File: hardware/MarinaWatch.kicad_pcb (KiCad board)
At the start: 2 copper layers, 45.4 x 40.5 mm, 18 parts, among them J1 USB_C_Receptacle_USB2.0_16P, J2 Screw_Terminal_01x02, U1 ESP32-S3-MINI-1, U2 MCP73831-2-OT, U3 AP2112K-3.3

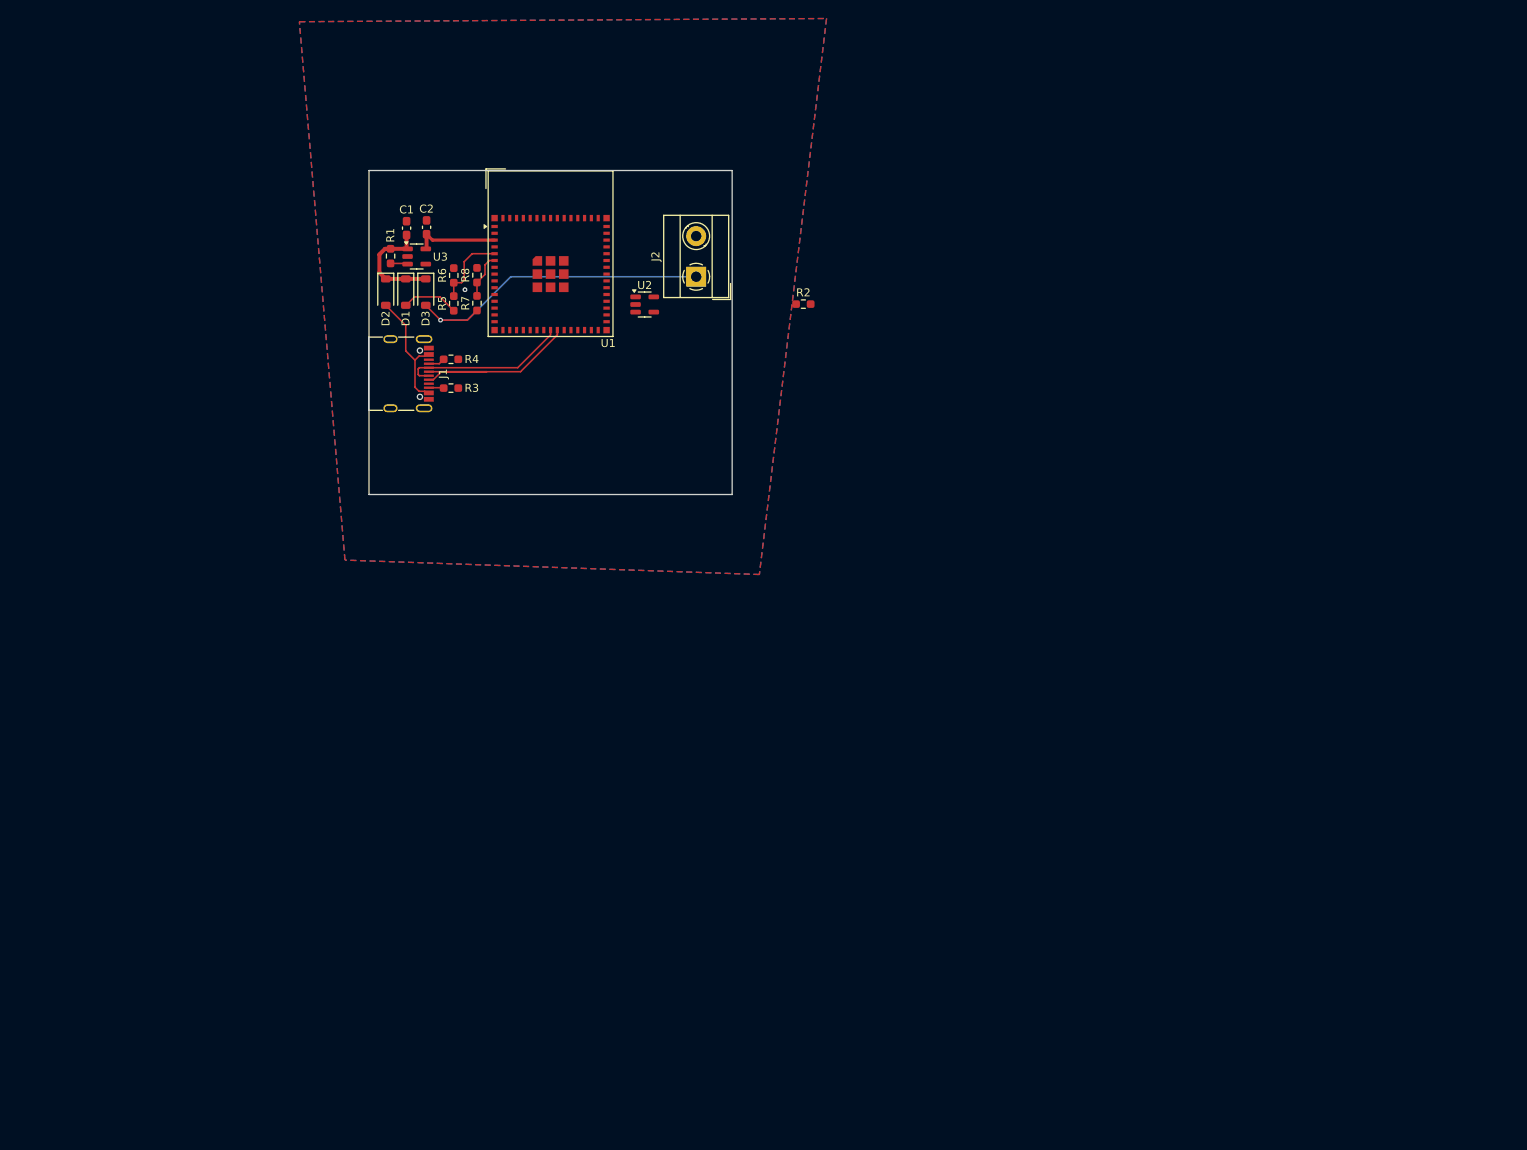
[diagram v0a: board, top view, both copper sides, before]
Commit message: Started with footprints and layout
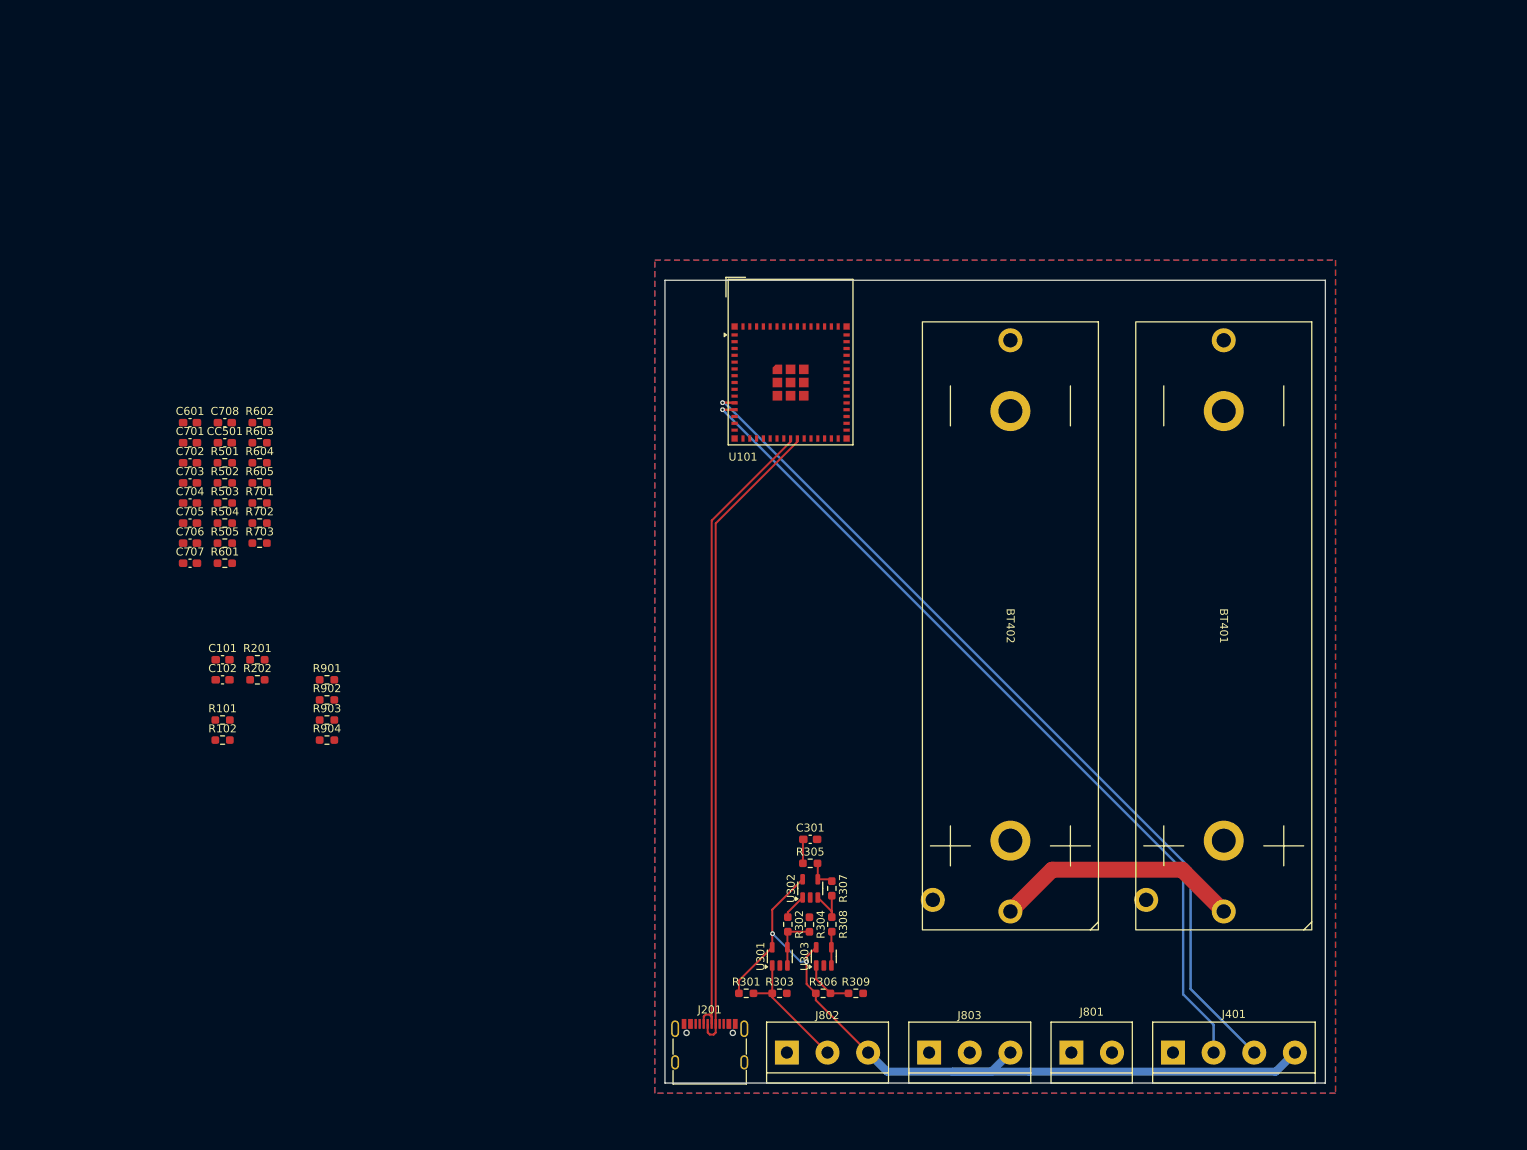
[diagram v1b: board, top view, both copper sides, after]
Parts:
- removed C1, C2: 10u, Capacitor_SMD:C_0603_1608Metric_Pad1.08x0.95mm_HandSolder
- removed D1, D2, D3: 1N5819, Diode_SMD:D_SOD-123
- removed J1: USB_C_Receptacle_USB2.0_16P, Connector_USB:USB_C_Receptacle_G-Switch_GT-USB-7010ASV
- removed J2: Screw_Terminal_01x02, TerminalBlock_MetzConnect:TerminalBlock_MetzConnect_Type101_RT01602HBWC_1x02_P5.08mm_Horizontal
- removed R1, R2: 12k, Resistor_SMD:R_0603_1608Metric_Pad0.98x0.95mm_HandSolder
- removed R3, R4, R5, R6, R7, R8: 5k1, Resistor_SMD:R_0603_1608Metric_Pad0.98x0.95mm_HandSolder
- removed U1: ESP32-S3-MINI-1, RF_Module:ESP32-S2-MINI-1
- removed U2: MCP73831-2-OT, Package_TO_SOT_SMD:SOT-23-5
- removed U3: AP2112K-3.3, Package_TO_SOT_SMD:SOT-23-5
- added BT401: Battery_Cell, AlfredLib:18650, F.Cu at (184.2, 96.5)
- added BT402: Battery_Cell, AlfredLib:18650, F.Cu at (157.5, 96.5)
- added C101: 10u, Capacitor_SMD:C_0603_1608Metric_Pad1.08x0.95mm_HandSolder, F.Cu at (59.0, 100.8)
- added C102: 10u, Capacitor_SMD:C_0603_1608Metric_Pad1.08x0.95mm_HandSolder, F.Cu at (59.0, 103.3)
- added C301: 22u, Capacitor_SMD:C_0603_1608Metric_Pad1.08x0.95mm_HandSolder, F.Cu at (132.5, 123.2)
- added C601: 10u, Capacitor_SMD:C_0603_1608Metric_Pad1.08x0.95mm_HandSolder, F.Cu at (54.9, 71.1)
- added C701: 10u, Capacitor_SMD:C_0603_1608Metric_Pad1.08x0.95mm_HandSolder, F.Cu at (54.9, 73.6)
- added C702: 10u, Capacitor_SMD:C_0603_1608Metric_Pad1.08x0.95mm_HandSolder, F.Cu at (54.9, 76.1)
- added C703: 10u, Capacitor_SMD:C_0603_1608Metric_Pad1.08x0.95mm_HandSolder, F.Cu at (54.9, 78.7)
- added C704: 10u, Capacitor_SMD:C_0603_1608Metric_Pad1.08x0.95mm_HandSolder, F.Cu at (54.9, 81.2)
- added C705: 22u, Capacitor_SMD:C_0603_1608Metric_Pad1.08x0.95mm_HandSolder, F.Cu at (54.9, 83.7)
- added C706: 22u, Capacitor_SMD:C_0603_1608Metric_Pad1.08x0.95mm_HandSolder, F.Cu at (54.9, 86.2)
- added C707: 22u, Capacitor_SMD:C_0603_1608Metric_Pad1.08x0.95mm_HandSolder, F.Cu at (54.9, 88.7)
- added C708: 100n, Capacitor_SMD:C_0603_1608Metric_Pad1.08x0.95mm_HandSolder, F.Cu at (59.3, 71.1)
- added CC501: 10u, Capacitor_SMD:C_0603_1608Metric_Pad1.08x0.95mm_HandSolder, F.Cu at (59.3, 73.6)
- added J201: USB_C_Receptacle_USB2.0_16P, Connector_USB:USB_C_Receptacle_G-Switch_GT-USB-7010ASV, F.Cu at (119.9, 150.0)
- added J401: Screw_Terminal_01x04, TerminalBlock:TerminalBlock_bornier-4_P5.08mm, F.Cu at (177.8, 149.9)
- added J801: Screw_Terminal_01x02, TerminalBlock:TerminalBlock_bornier-2_P5.08mm, F.Cu at (165.1, 149.9)
- added J802: Screw_Terminal_01x03, TerminalBlock:TerminalBlock_bornier-3_P5.08mm, F.Cu at (129.5, 149.9)
- added J803: Screw_Terminal_01x03, TerminalBlock:TerminalBlock_bornier-3_P5.08mm, F.Cu at (147.3, 149.9)
- added R101: 5k1, Resistor_SMD:R_0603_1608Metric_Pad0.98x0.95mm_HandSolder, F.Cu at (59.0, 108.3)
- added R102: 5k1, Resistor_SMD:R_0603_1608Metric_Pad0.98x0.95mm_HandSolder, F.Cu at (59.0, 110.8)
- added R201: 5k1, Resistor_SMD:R_0603_1608Metric_Pad0.98x0.95mm_HandSolder, F.Cu at (63.4, 100.8)
- added R202: 5k1, Resistor_SMD:R_0603_1608Metric_Pad0.98x0.95mm_HandSolder, F.Cu at (63.4, 103.3)
- added R301: 120R, Resistor_SMD:R_0603_1608Metric_Pad0.98x0.95mm_HandSolder, F.Cu at (124.5, 142.4)
- added R302: 200R, Resistor_SMD:R_0603_1608Metric_Pad0.98x0.95mm_HandSolder, F.Cu at (129.7, 133.8)
- added R303: 90R, Resistor_SMD:R_0603_1608Metric_Pad0.98x0.95mm_HandSolder, F.Cu at (128.6, 142.4)
- added R304: 1k5, Resistor_SMD:R_0603_1608Metric_Pad0.98x0.95mm_HandSolder, F.Cu at (132.4, 133.8)
- added R305: 100R, Resistor_SMD:R_0603_1608Metric_Pad0.98x0.95mm_HandSolder, F.Cu at (132.5, 126.2)
- added R306: 120R, Resistor_SMD:R_0603_1608Metric_Pad0.98x0.95mm_HandSolder, F.Cu at (134.1, 142.4)
- added R307: 1k5, Resistor_SMD:R_0603_1608Metric_Pad0.98x0.95mm_HandSolder, F.Cu at (135.2, 129.3)
- added R308: 200R, Resistor_SMD:R_0603_1608Metric_Pad0.98x0.95mm_HandSolder, F.Cu at (135.2, 133.8)
- added R309: 90R, Resistor_SMD:R_0603_1608Metric_Pad0.98x0.95mm_HandSolder, F.Cu at (138.2, 142.4)
- added R501: 0R, Resistor_SMD:R_0603_1608Metric_Pad0.98x0.95mm_HandSolder, F.Cu at (59.3, 76.1)
- added R502: 5k1, Resistor_SMD:R_0603_1608Metric_Pad0.98x0.95mm_HandSolder, F.Cu at (59.3, 78.7)
- added R503: 5k1, Resistor_SMD:R_0603_1608Metric_Pad0.98x0.95mm_HandSolder, F.Cu at (59.3, 81.2)
- added R504: 5k1, Resistor_SMD:R_0603_1608Metric_Pad0.98x0.95mm_HandSolder, F.Cu at (59.3, 83.7)
- added R505: 5k1, Resistor_SMD:R_0603_1608Metric_Pad0.98x0.95mm_HandSolder, F.Cu at (59.3, 86.2)
- added R601: 0R, Resistor_SMD:R_0603_1608Metric_Pad0.98x0.95mm_HandSolder, F.Cu at (59.3, 88.7)
- added R602: 5k1, Resistor_SMD:R_0603_1608Metric_Pad0.98x0.95mm_HandSolder, F.Cu at (63.6, 71.1)
- added R603: 5k1, Resistor_SMD:R_0603_1608Metric_Pad0.98x0.95mm_HandSolder, F.Cu at (63.6, 73.6)
- added R604: 5k1, Resistor_SMD:R_0603_1608Metric_Pad0.98x0.95mm_HandSolder, F.Cu at (63.6, 76.1)
- added R605: 5k1, Resistor_SMD:R_0603_1608Metric_Pad0.98x0.95mm_HandSolder, F.Cu at (63.6, 78.7)
- added R701: 5k1, Resistor_SMD:R_0603_1608Metric_Pad0.98x0.95mm_HandSolder, F.Cu at (63.6, 81.2)
- added R702: 470k, Resistor_SMD:R_0603_1608Metric_Pad0.98x0.95mm_HandSolder, F.Cu at (63.6, 83.7)
- added R703: 150k, Resistor_SMD:R_0603_1608Metric_Pad0.98x0.95mm_HandSolder, F.Cu at (63.6, 86.2)
- added R901: 3k, Resistor_SMD:R_0603_1608Metric_Pad0.98x0.95mm_HandSolder, F.Cu at (72.0, 103.3)
- added R902: 3k, Resistor_SMD:R_0603_1608Metric_Pad0.98x0.95mm_HandSolder, F.Cu at (72.0, 105.8)
- added R903: 7k5, Resistor_SMD:R_0603_1608Metric_Pad0.98x0.95mm_HandSolder, F.Cu at (72.0, 108.3)
- added R904: 7k5, Resistor_SMD:R_0603_1608Metric_Pad0.98x0.95mm_HandSolder, F.Cu at (72.0, 110.8)
- added U101: ESP32-S3-MINI-1, RF_Module:ESP32-S2-MINI-1, F.Cu at (130.0, 63.5)
- added U301: LMV321, Package_TO_SOT_SMD:SOT-23-5, F.Cu at (128.7, 137.8)
- added U302: LMV321, Package_TO_SOT_SMD:SOT-23-5, F.Cu at (132.5, 129.3)
- added U303: LMV321, Package_TO_SOT_SMD:SOT-23-5, F.Cu at (134.2, 137.8)
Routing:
- net /I2C_SDA: track 0.00 -> 110.6 mm, vias 0 -> 1
- net /I2C_SCL: track 0.00 -> 107.5 mm, vias 0 -> 1
- net +3V3: track 10.7 -> 103.7 mm, vias 0 -> 2
- net /D-: track 20.7 -> 80.3 mm
- net /D+: track 26.8 -> 80.8 mm
- net SOLAR: track 41.9 -> 0.00 mm, vias 1 -> 0
- net +BATT: track 7.22 -> 31.0 mm
- net /PT100: track 0.00 -> 16.1 mm
- net VBUS: track 15.2 -> 0.00 mm
- net VCC: track 14.0 -> 0.00 mm
- net /V_BAT: track 9.62 -> 0.00 mm
- net /TEMP_DIFF+: track 0.00 -> 6.95 mm
- net /TEMP_REF: track 0.00 -> 6.47 mm
- net /AMP-: track 0.00 -> 5.85 mm
- net /V_SOLAR: track 5.72 -> 0.00 mm
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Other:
- board size 45.4 x 40.5 mm -> 82.5 x 100.3 mm

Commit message: Working on power circuitry layout
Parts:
- removed J803: Screw_Terminal_01x03, TerminalBlock:TerminalBlock_bornier-3_P5.08mm
- added L701: 1u5, Inductor_SMD_Wurth:L_Wurth_WE-LQSH-2010, F.Cu at (138.1, 94.0)
- added R801: 100R, Resistor_SMD:R_0603_1608Metric_Pad0.98x0.95mm_HandSolder, F.Cu at (136.6, 133.0)
- added R802: 100R, Resistor_SMD:R_0603_1608Metric_Pad0.98x0.95mm_HandSolder, F.Cu at (132.4, 133.0)
- added U501: BQ24210, AlfredLib:WSON-10, F.Cu at (138.4, 100.8)
- added U601: BQ24210, AlfredLib:WSON-10, F.Cu at (138.4, 106.6)
- added U701: TPS63070, AlfredLib:VQFN-3.0x2.5, F.Cu at (138.1, 90.0)
- moved C101 95.7 mm to (146.7, 62.5)
- moved R101 95.7 mm to (146.7, 70.0)
- moved C701 93.8 mm to (147.0, 91.4), turned to -90 degrees
- moved C702 91.5 mm to (145.1, 91.4), turned to -90 degrees
- moved C703 89.3 mm to (143.3, 91.4), turned to -90 degrees
- moved R501 86.2 mm to (142.5, 98.7)
- moved C601 86.1 mm to (134.2, 104.5), turned to 180 degrees
- moved R603 85.9 mm to (142.4, 107.9)
- moved R503 85.8 mm to (142.5, 102.1)
- moved R601 84.6 mm to (142.4, 104.5)
- moved R505 84.4 mm to (142.5, 100.4)
- moved R605 83.5 mm to (142.4, 106.2)
- moved C704 80.7 mm to (134.9, 92.0), turned to -90 degrees
- moved R602 79.6 mm to (134.2, 107.9)
- moved C501 79.0 mm to (134.2, 98.6), turned to 180 degrees
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- renumbered CC501 to C501
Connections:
- net Net-(U701-FB) renamed /POWER/FB
- C601 pad 2: Net-(U601-VSS) -> GND
- C708 pad 1: Net-(U701-VAUX) -> /POWER/VAUX
- J802 pad 2: /PT100 -> /SIG
- R501 pad 1: Net-(U501-BAT) -> /POWER/USB_BAT
- R502 pad 1: Net-(U501-VTSB) -> /POWER/USB_VTSB
- R502 pad 2: Net-(U501-TS) -> /POWER/USB_TS
- R503 pad 1: Net-(U501-~{EN}) -> /POWER/USB_EN
- R504 pad 1: Net-(U501-ISET) -> /POWER/USB_ISET
- R505 pad 1: Net-(U501-VDPM) -> /POWER/USB_VDPM
- R601 pad 1: Net-(U601-BAT) -> /POWER/SOLAR_BAT
- R602 pad 1: Net-(U601-VTSB) -> /POWER/SOLAR_VTSB
- R602 pad 2: Net-(U601-TS) -> /POWER/SOLAR_TS
- R603 pad 1: Net-(U601-~{EN}) -> /POWER/SOLAR_EN
- R603 pad 2: Net-(U601-VSS) -> GND
- R604 pad 1: Net-(U601-ISET) -> /POWER/SOLAR_ISET
- R604 pad 2: Net-(U601-VSS) -> GND
- R605 pad 1: Net-(U601-VDPM) -> /POWER/SOLAR_VDPM
- R605 pad 2: Net-(U601-VSS) -> GND
- R701 pad 2: Net-(U701-EN) -> /POWER/EN
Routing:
- net SOLAR: track 0.00 -> 64.9 mm, vias 0 -> 1
- net VBUS: track 0.00 -> 52.1 mm, vias 0 -> 1
- net +BATT: track 31.0 -> 79.8 mm
- net +3V3: track 103.7 -> 67.4 mm
- net /SIG: track 0.00 -> 27.5 mm
- net /PT100: track 16.1 -> 7.74 mm
- net /POWER/VAUX: track 0.00 -> 4.90 mm
- net /POWER/USB_VTSB: track 0.00 -> 4.44 mm
- net /POWER/SOLAR_VTSB: track 0.00 -> 4.41 mm
- net /POWER/EN: track 0.00 -> 3.85 mm
- net /D+: track 80.8 -> 84.6 mm
- net /POWER/FB: track 0.00 -> 3.60 mm
- net /D-: track 80.3 -> 83.2 mm
- net /I2C_SCL: track 107.5 -> 104.7 mm
- net /I2C_SDA: track 110.6 -> 108.0 mm
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- added copper zone on F.Cu, net +3V3
- added copper zone on F.Cu, net +BATT
- added copper zone on F.Cu, net /POWER/L1
- added copper zone on F.Cu, net /POWER/L2
- added copper zone on F.Cu, net /POWER/SOLAR_BAT
- added copper zone on F.Cu, net /POWER/USB_BAT
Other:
- board size 82.5 x 100.3 mm -> 70 x 101 mm
- board text added: "SCL"
- board text added: "SDA"
- board text added: "SIG"
